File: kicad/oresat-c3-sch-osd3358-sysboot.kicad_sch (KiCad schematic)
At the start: 26 parts, among them J6 Conn_01x02, U1 OSD3358-512M-BSM

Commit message: Zero airwires! Rough draft schematic and layout are done. Still need ERC and DRC and full design review and stiching and polish.
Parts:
- removed TP122, TP124, TP25, TP86, TP87: Test-Point, oresat-misc:TestPoint_Pad_D1.0mm, symbol oresat-misc:Test-Point-1mm-round
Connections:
- net LBAND_LO_nSEN: now reaches U1.H16 (MII1_TX_CLK)
- net RADIO_ENABLE: now reaches U1.F3 (LCD_VSYNC)
- net LBAND_LO_SDATA: now reaches U1.H14 (MII1_TXD1)
- net LBAND_LO_SCLK: now reaches U1.H15 (MII1_TXD0)
- net LBAND_LO_nLOCKED: now reaches U1.J14 (RMII1_REF_CLK)
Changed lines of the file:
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@@
+    (stroke (width 0) (type default))
+  )
+  (wire (pts (xy 101.6 134.62) (xy 116.84 134.62))
     (stroke (width 0) (type default))
   )
@@
     (stroke (width 0) (type default))
   )
-  (wire (pts (xy 114.3 129.54) (xy 116.84 129.54))
-    (stroke (width 0) (type default))
-  )
   (wire (pts (xy 116.84 154.94) (xy 114.3 154.94))
     (stroke (width 0) (type default))
@@
     (stroke (width 0) (type default))
   )
+  (wire (pts (xy 101.6 129.54) (xy 116.84 129.54))
+    (stroke (width 0) (type default))
+  )
   (wire (pts (xy 114.3 157.48) (xy 116.84 157.48))
     (stroke (width 0) (type default))
@@
     (stroke (width 0) (type default))
   )
-  (wire (pts (xy 114.3 172.72) (xy 116.84 172.72))
+  (wire (pts (xy 102.87 172.72) (xy 116.84 172.72))
     (stroke (width 0) (type default))
   )
@@
     (stroke (width 0) (type default))
   )
-  (wire (pts (xy 114.3 134.62) (xy 116.84 134.62))
-    (stroke (width 0) (type default))
-  )
   (wire (pts (xy 210.82 134.62) (xy 210.82 120.65))
     (stroke (width 0) (type default))
@@
     (stroke (width 0) (type default))
   )
-  (wire (pts (xy 114.3 132.08) (xy 116.84 132.08))
-    (stroke (width 0) (type default))
-  )
   (wire (pts (xy 177.8 137.16) (xy 213.36 137.16))
     (stroke (width 0) (type default))
@@
   )
   (wire (pts (xy 116.84 175.26) (xy 114.3 175.26))
+    (stroke (width 0) (type default))
+  )
+  (wire (pts (xy 101.6 132.08) (xy 116.84 132.08))
     (stroke (width 0) (type default))
   )
@@
   (text "0" (at 186.69 129.54 0)
     (effects (font (size 1.27 1.27)) (justify right bottom))
+  )
+  (global_label "LBAND_LO_nSEN" (shape output) (at 101.6 129.54 180) (fields_autoplaced)
+    (effects (font (size 1.27 1.27) (thickness 0.254) bold) (justify right))
+    (property "Intersheetrefs" "${INTERSHEET_REFS}" (at 83.1468 129.54 0)
+      (effects (font (size 1.27 1.27)) (justify right))
+    )
+  )
+  (global_label "LBAND_LO_SDATA" (shape output) (at 101.6 134.62 180) (fields_autoplaced)
+    (effects (font (size 1.27 1.27) (thickness 0.254) bold) (justify right))
+    (property "Intersheetrefs" "${INTERSHEET_REFS}" (at 82.3605 134.62 0)
+      (effects (font (size 1.27 1.27)) (justify right))
+    )
+  )
+  (global_label "LBAND_LO_nLOCKED" (shape input) (at 102.87 172.72 180) (fields_autoplaced)
+    (effects (font (size 1.27 1.27) (thickness 0.254) bold) (justify right))
+    (property "Intersheetrefs" "${INTERSHEET_REFS}" (at 80.7882 172.72 0)
+      (effects (font (size 1.27 1.27)) (justify right))
+    )
+  )
+  (global_label "LBAND_LO_SCLK" (shape output) (at 101.6 132.08 180) (fields_autoplaced)
+    (effects (font (size 1.27 1.27) (thickness 0.254) bold) (justify right))
+    (property "Intersheetrefs" "${INTERSHEET_REFS}" (at 83.2072 132.08 0)
+      (effects (font (size 1.27 1.27)) (justify right))
+    )
   )
   (global_label "PET_WDT" (shape input) (at 180.34 180.34 0) (fields_autoplaced)
@@
     )
   )
+  (global_label "RADIO_ENABLE" (shape input) (at 180.34 175.26 0) (fields_autoplaced)
+    (effects (font (size 1.27 1.27)) (justify left))
+    (property "Intersheetrefs" "${INTERSHEET_REFS}" (at 196.7925 175.26 0)
+      (effects (font (size 1.27 1.27)) (justify left))
+    )
+  )
   (symbol (lib_id "oresat-misc:Test-Point-1mm-round") (at 114.3 162.56 270) (unit 1)
     (in_bom yes) (on_board yes) (dnp no)
@@
   (symbol (lib_id "power:GND") (at 220.98 193.04 0) (unit 1)
     (in_bom yes) (on_board yes) (dnp no)
-    (property "Reference" "#PWR?" (at 220.98 199.39 0)
+    (property "Reference" "#PWR0161" (at 220.98 199.39 0)
       (effects (font (size 1.27 1.27)) hide)
     )
@@
       (project "oresat-c3"
         (path "/65d12cdd-c326-4033-9053-c59fa4e0b25e/0c732c1e-ab0d-41ac-9d77-9d7763333b6f"
-          (reference "#PWR?") (unit 1)
+          (reference "#PWR0161") (unit 1)
         )
       )
@@
     )
   )
-  (symbol (lib_id "oresat-misc:Test-Point-1mm-round") (at 114.3 129.54 270) (unit 1)
-    (in_bom yes) (on_board yes) (dnp no)
-    (property "Reference" "TP25" (at 105.41 129.54 90)
-      (effects (font (size 1.27 1.27)) (justify left))
-    )
-    (property "Value" "Test-Point" (at 116.84 129.54 0)
-      (effects (font (size 1.27 1.27)) hide)
-    )
-    (property "Footprint" "oresat-misc:TestPoint_Pad_D1.0mm" (at 124.46 129.54 0)
-      (effects (font (size 1.27 1.27)) hide)
-    )
-    (property "Datasheet" "" (at 114.3 129.54 0)
-      (effects (font (size 1.27 1.27)) hide)
-    )
-    (pin "1")
-    (instances
-      (project "oresat-c3"
-        (path "/65d12cdd-c326-4033-9053-c59fa4e0b25e/0c732c1e-ab0d-41ac-9d77-9d7763333b6f"
-          (reference "TP25") (unit 1)
-        )
-      )
-    )
-  )
   (symbol (lib_id "oresat-misc:Test-Point-1mm-round") (at 114.3 157.48 270) (unit 1)
     (in_bom yes) (on_board yes) (dnp no)
@@
         (path "/65d12cdd-c326-4033-9053-c59fa4e0b25e/0c732c1e-ab0d-41ac-9d77-9d7763333b6f"
           (reference "TP123") (unit 1)
-        )
-      )
-    )
-  )
-  (symbol (lib_id "oresat-misc:Test-Point-1mm-round") (at 180.34 175.26 90) (unit 1)
-    (in_bom yes) (on_board yes) (dnp no)
-    (property "Reference" "TP124" (at 189.23 175.26 90)
-      (effects (font (size 1.27 1.27)) (justify left))
-    )
-    (property "Value" "Test-Point" (at 177.8 175.26 0)
-      (effects (font (size 1.27 1.27)) hide)
-    )
-    (property "Footprint" "oresat-misc:TestPoint_Pad_D1.0mm" (at 170.18 175.26 0)
-      (effects (font (size 1.27 1.27)) hide)
-    )
-    (property "Datasheet" "" (at 180.34 175.26 0)
-      (effects (font (size 1.27 1.27)) hide)
-    )
-    (pin "1")
-    (instances
-      (project "oresat-c3"
-        (path "/65d12cdd-c326-4033-9053-c59fa4e0b25e/0c732c1e-ab0d-41ac-9d77-9d7763333b6f"
-          (reference "TP124") (unit 1)
         )
       )
@@
     )
   )
-  (symbol (lib_id "oresat-misc:Test-Point-1mm-round") (at 114.3 172.72 270) (unit 1)
-    (in_bom yes) (on_board yes) (dnp no)
-    (property "Reference" "TP122" (at 105.41 172.72 90)
-      (effects (font (size 1.27 1.27)) (justify left))
-    )
-    (property "Value" "Test-Point" (at 116.84 172.72 0)
-      (effects (font (size 1.27 1.27)) hide)
-    )
-    (property "Footprint" "oresat-misc:TestPoint_Pad_D1.0mm" (at 124.46 172.72 0)
-      (effects (font (size 1.27 1.27)) hide)
-    )
-    (property "Datasheet" "" (at 114.3 172.72 0)
-      (effects (font (size 1.27 1.27)) hide)
-    )
-    (pin "1")
-    (instances
-      (project "oresat-c3"
-        (path "/65d12cdd-c326-4033-9053-c59fa4e0b25e/0c732c1e-ab0d-41ac-9d77-9d7763333b6f"
-          (reference "TP122") (unit 1)
-        )
-      )
-    )
-  )
   (symbol (lib_id "Connector_Generic:Conn_01x02") (at 254 134.62 0) (unit 1)
     (in_bom yes) (on_board yes) (dnp no)
@@
     )
   )
-  (symbol (lib_id "oresat-misc:Test-Point-1mm-round") (at 114.3 132.08 270) (unit 1)
-    (in_bom yes) (on_board yes) (dnp no)
-    (property "Reference" "TP86" (at 105.41 132.08 90)
-      (effects (font (size 1.27 1.27)) (justify left))
-    )
-    (property "Value" "Test-Point" (at 116.84 132.08 0)
-      (effects (font (size 1.27 1.27)) hide)
-    )
-    (property "Footprint" "oresat-misc:TestPoint_Pad_D1.0mm" (at 124.46 132.08 0)
-      (effects (font (size 1.27 1.27)) hide)
-    )
-    (property "Datasheet" "" (at 114.3 132.08 0)
-      (effects (font (size 1.27 1.27)) hide)
-    )
-    (pin "1")
-    (instances
-      (project "oresat-c3"
-        (path "/65d12cdd-c326-4033-9053-c59fa4e0b25e/0c732c1e-ab0d-41ac-9d77-9d7763333b6f"
-          (reference "TP86") (unit 1)
-        )
-      )
-    )
-  )
   (symbol (lib_id "power:GND") (at 248.92 139.7 0) (unit 1)
     (in_bom yes) (on_board yes) (dnp no)
-    (property "Reference" "#PWR?" (at 248.92 146.05 0)
+    (property "Reference" "#PWR0160" (at 248.92 146.05 0)
       (effects (font (size 1.27 1.27)) hide)
     )
@@
       (project "oresat-c3"
         (path "/65d12cdd-c326-4033-9053-c59fa4e0b25e/0c732c1e-ab0d-41ac-9d77-9d7763333b6f"
-          (reference "#PWR?") (unit 1)
-        )
-      )
-    )
-  )
-  (symbol (lib_id "oresat-misc:Test-Point-1mm-round") (at 114.3 134.62 270) (unit 1)
-    (in_bom yes) (on_board yes) (dnp no)
-    (property "Reference" "TP87" (at 105.41 134.62 90)
-      (effects (font (size 1.27 1.27)) (justify left))
-    )
-    (property "Value" "Test-Point" (at 116.84 134.62 0)
-      (effects (font (size 1.27 1.27)) hide)
-    )
-    (property "Footprint" "oresat-misc:TestPoint_Pad_D1.0mm" (at 124.46 134.62 0)
-      (effects (font (size 1.27 1.27)) hide)
-    )
-    (property "Datasheet" "" (at 114.3 134.62 0)
-      (effects (font (size 1.27 1.27)) hide)
-    )
-    (pin "1")
-    (instances
-      (project "oresat-c3"
-        (path "/65d12cdd-c326-4033-9053-c59fa4e0b25e/0c732c1e-ab0d-41ac-9d77-9d7763333b6f"
-          (reference "TP87") (unit 1)
-        )
-      )
+          (reference "#PWR0160") (unit 1)
+        )
+      )

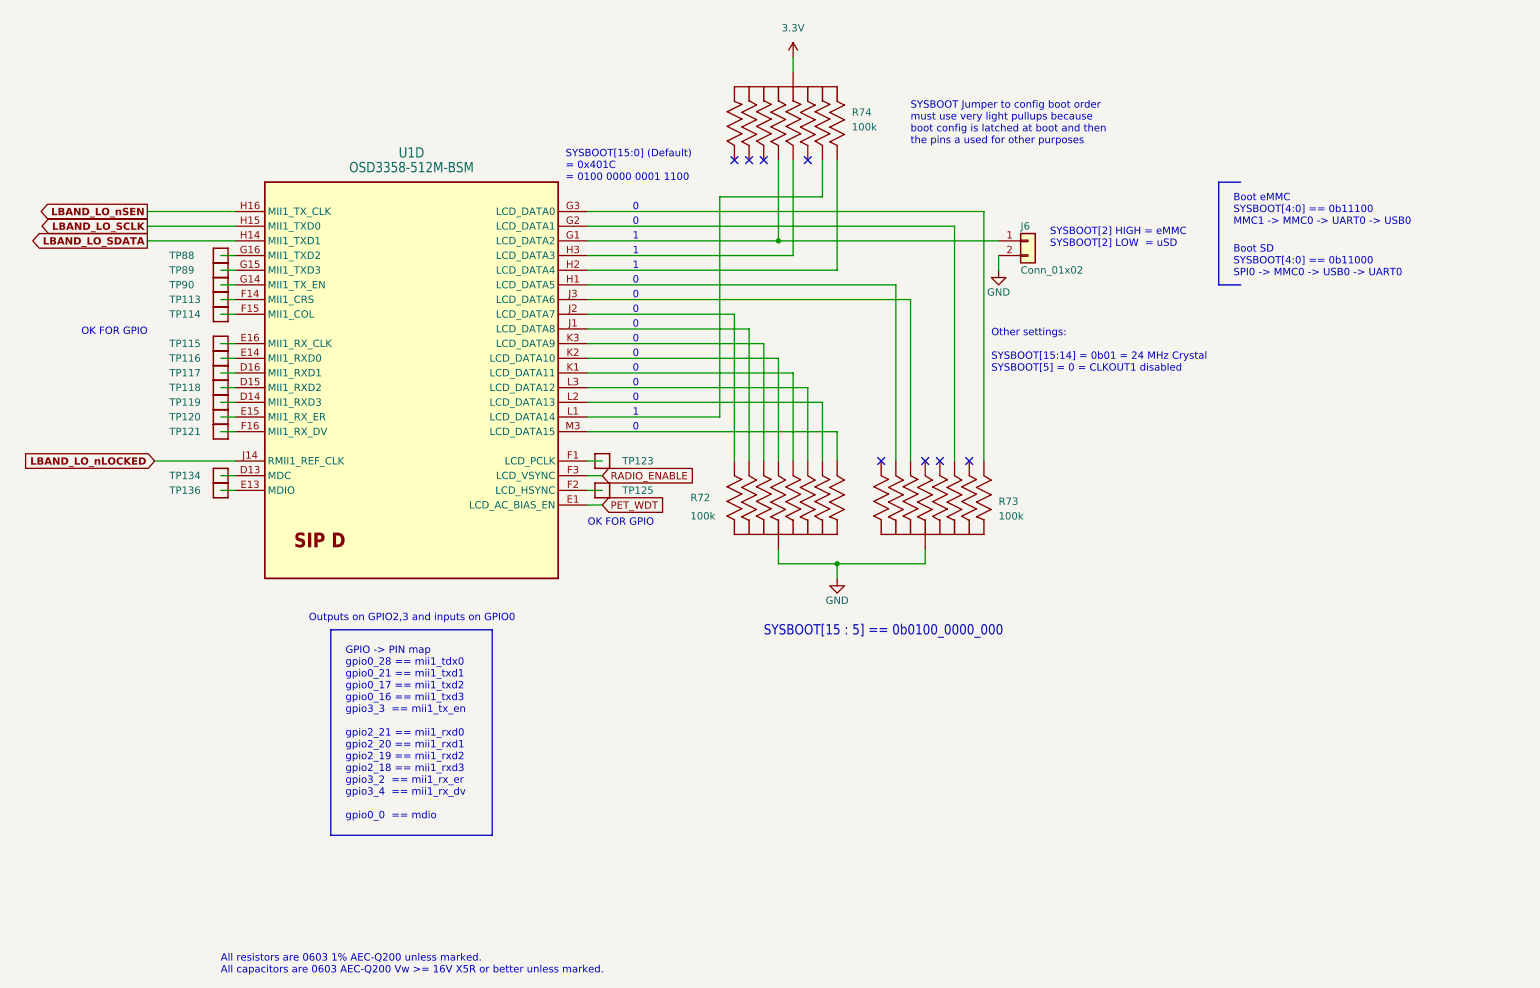
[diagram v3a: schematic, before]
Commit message: Added reset states of GPIO lines to OSD3358 pins in schematic so we know what pulls up unexpectedly. Re-arranged a few pins that should not pull up on boot.
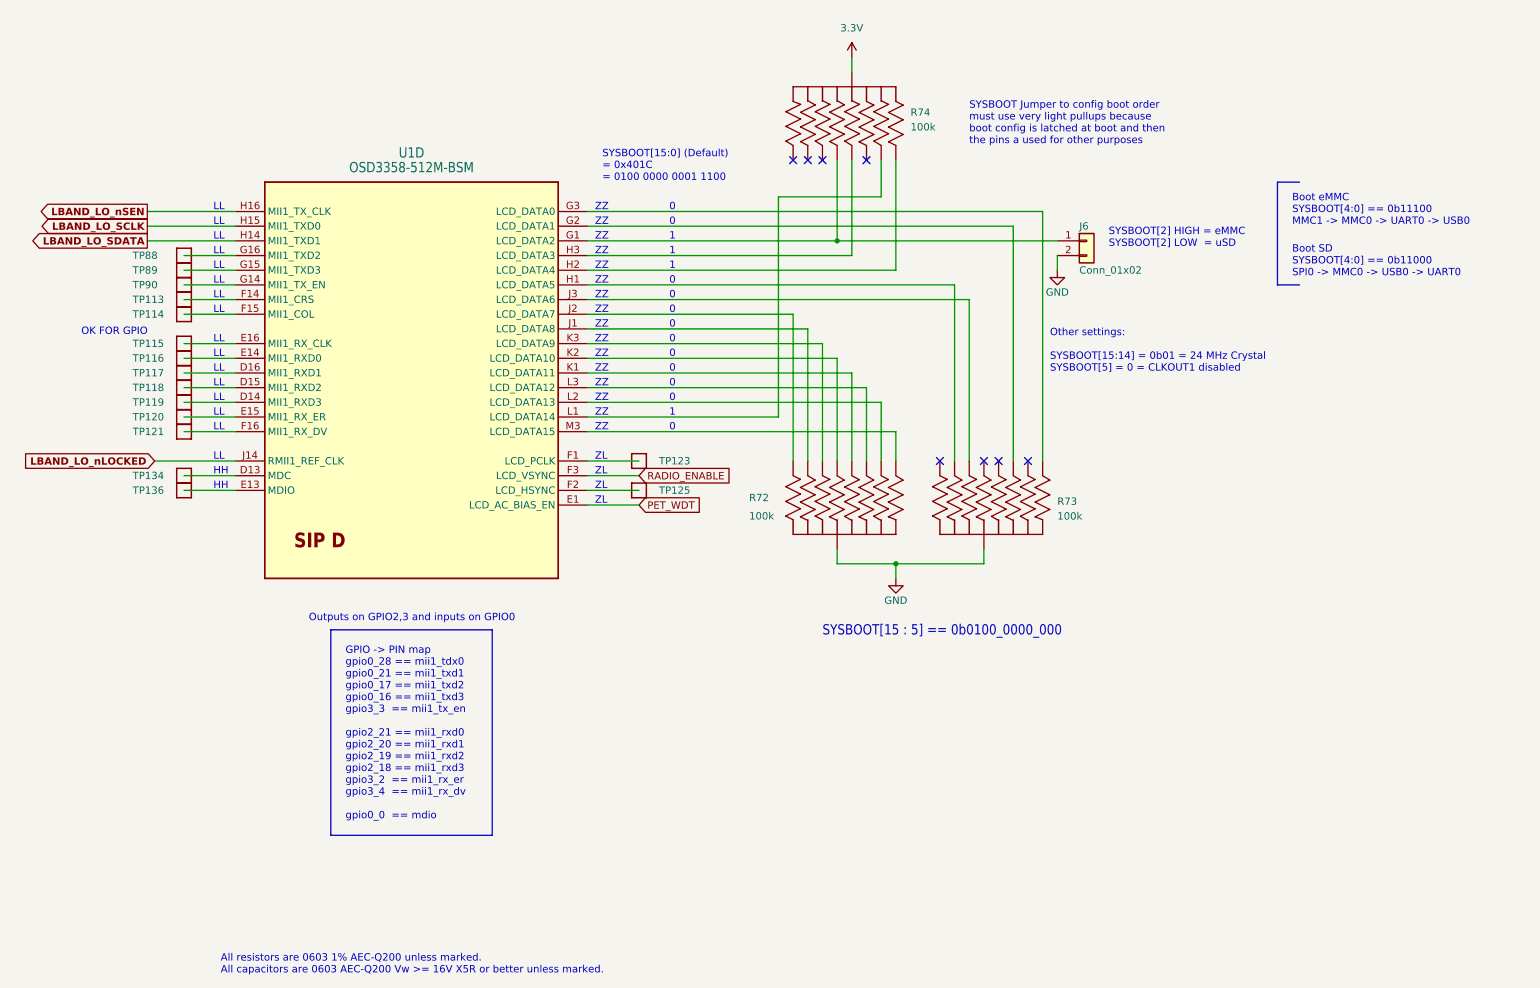
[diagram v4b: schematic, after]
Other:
- note added: "HH"
- note added: "LL"
- note added: "ZL"
- note added: "ZZ"
- moved on the sheet: J6, R72, R73, R74, TP113, TP114, TP115, TP116, TP117, TP118, TP119, TP120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
